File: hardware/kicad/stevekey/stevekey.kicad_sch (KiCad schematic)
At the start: 24 parts, among them J1 ATMEL-ICE-10, J2 Conn_01x04, J3 Conn_01x02, J4 Conn_01x02, J5 Conn_01x02, Q1 2N3904, SW1 SW_SL, SW2 SW_CAPS, SW3 SW_4080, U1 CD4066BM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

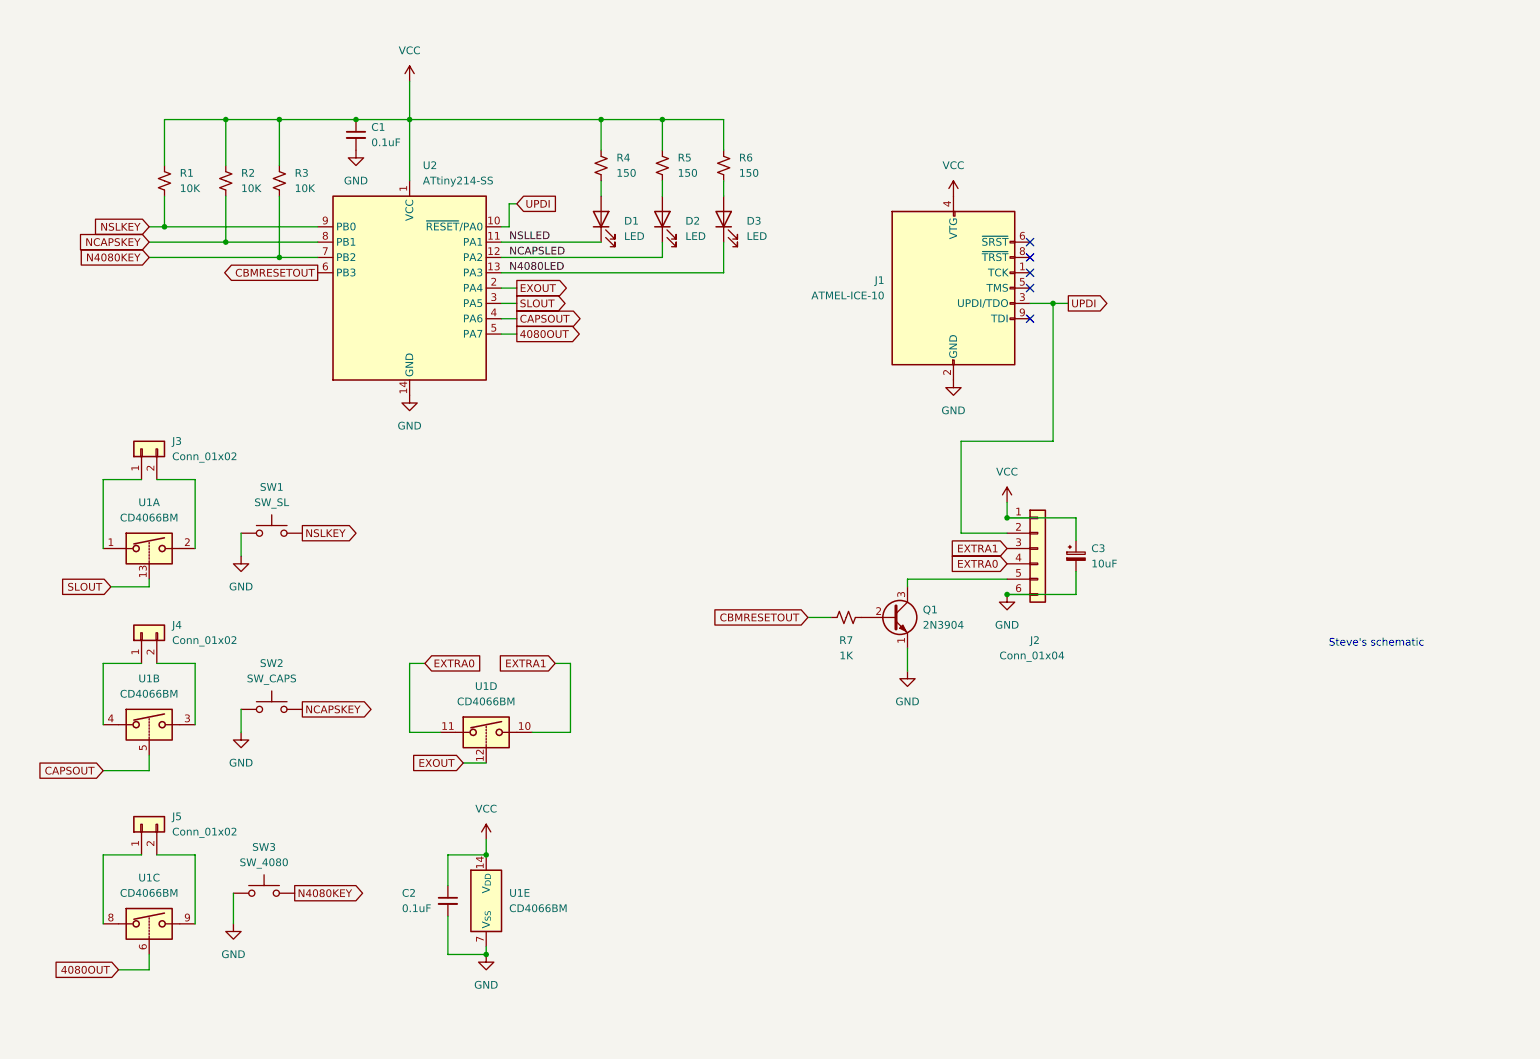
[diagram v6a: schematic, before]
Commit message: Use 330 ohm resistor for LEDs
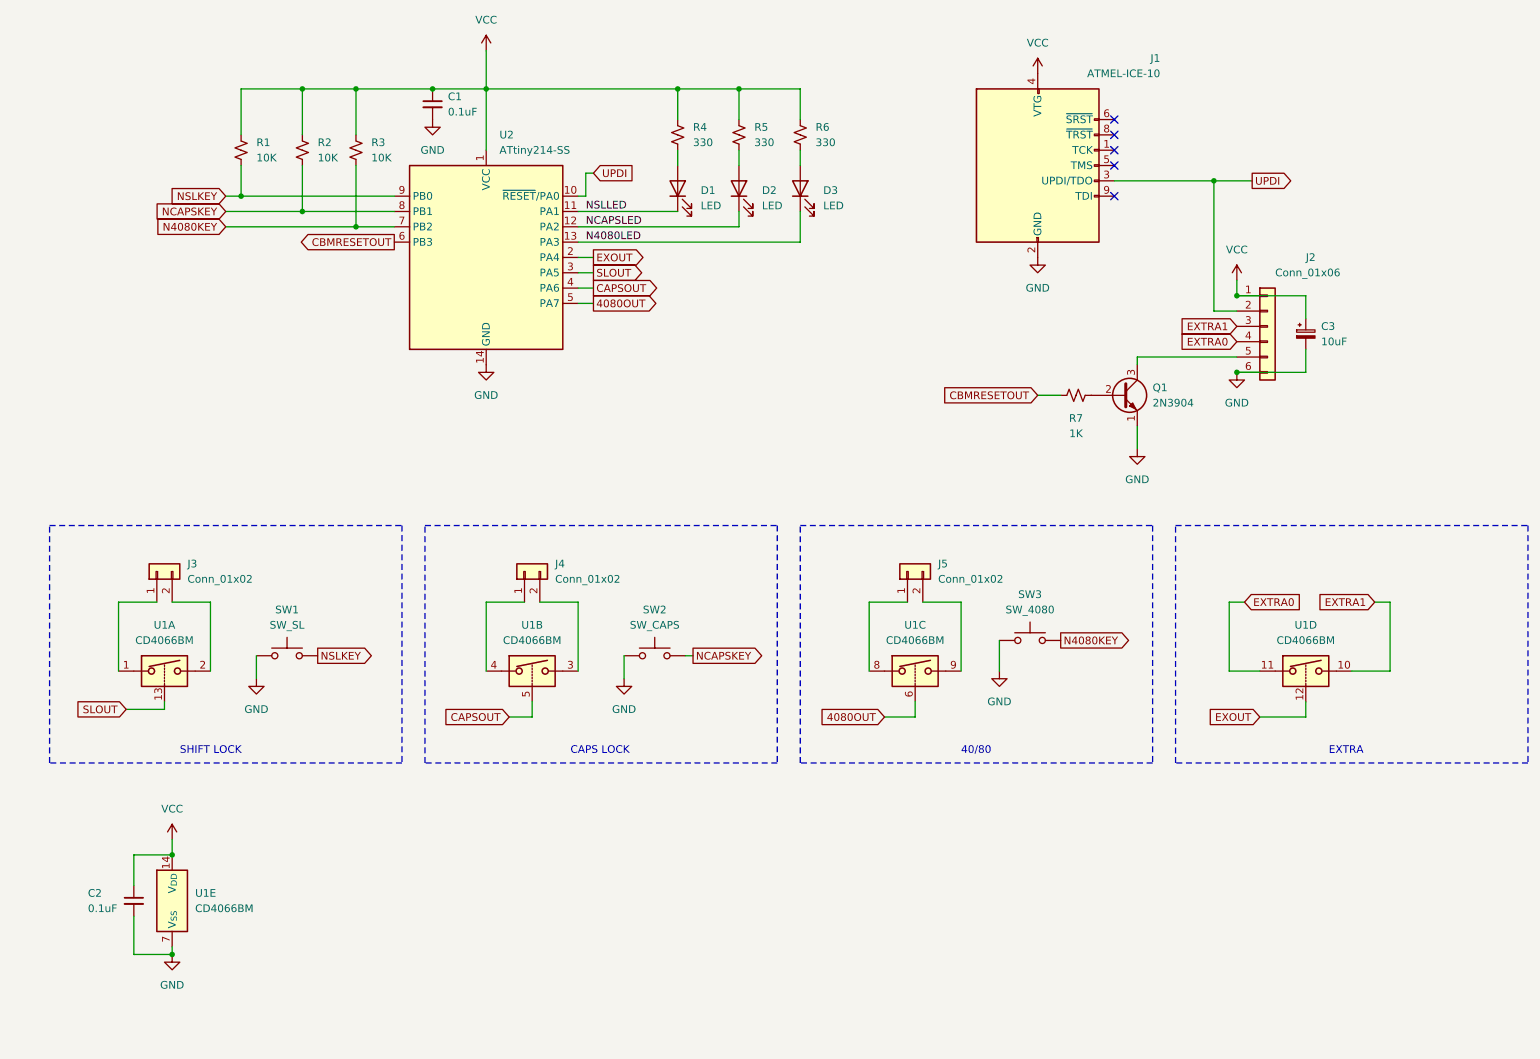
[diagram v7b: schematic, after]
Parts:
- J2: value Conn_01x04 -> Conn_01x06
- R4, R5, R6: value 150 -> 330
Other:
- note added: "40/80"
- note added: "CAPS LOCK"
- note added: "EXTRA"
- note added: "SHIFT LOCK"
- note removed: "Steve's schematic"
- moved on the sheet: C1, C2, C3, D1, D2, D3, J1, J2, J3, J4, J5, Q1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

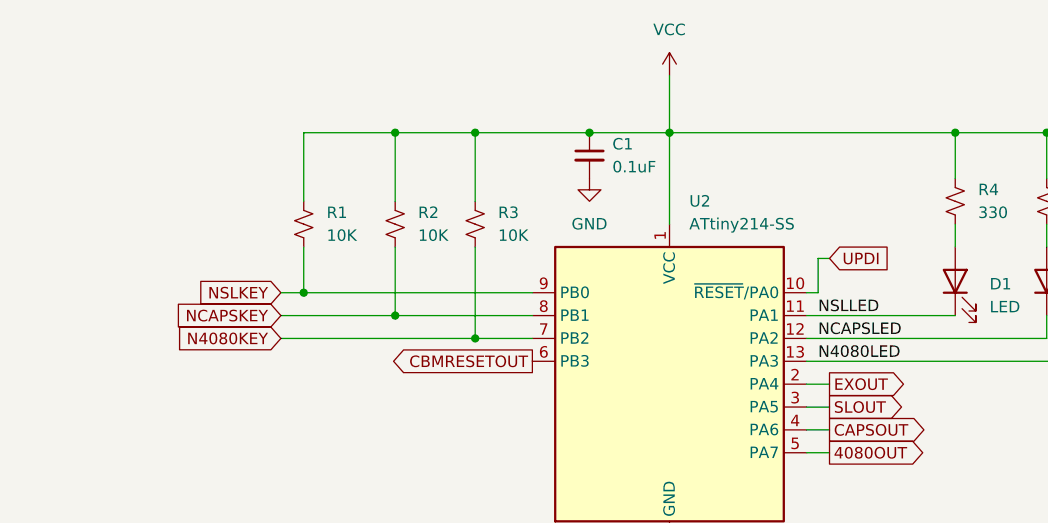
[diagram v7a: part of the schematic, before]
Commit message: Use internal pull-ups for keys
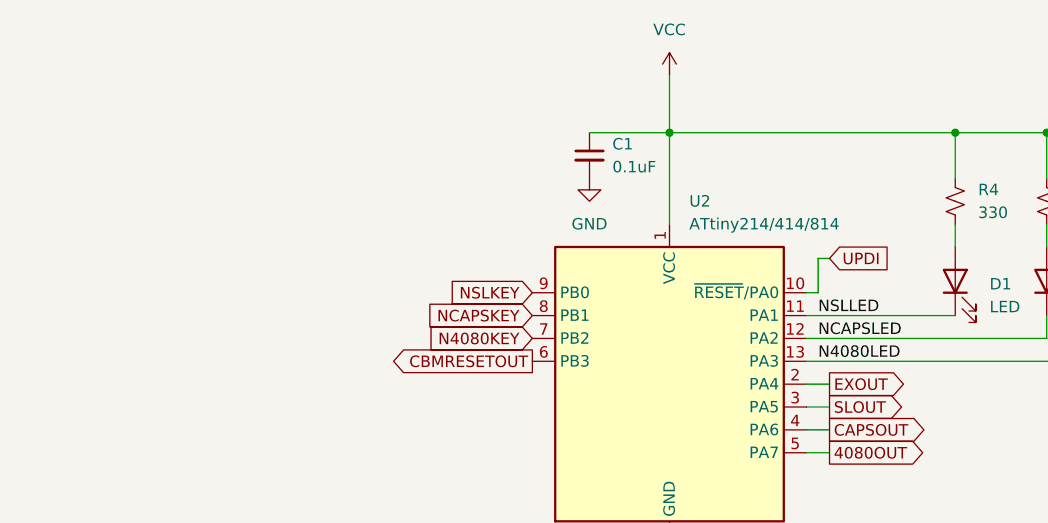
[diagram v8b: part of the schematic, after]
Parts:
- removed R1, R2, R3: 10K, Resistor_THT:R_Axial_DIN0204_L3.6mm_D1.6mm_P7.62mm_Horizontal, symbol Device:R_Small_US
- U2: value ATtiny214-SS -> ATtiny214/414/814
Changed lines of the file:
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@@
 (kicad_sch (version 20230121) (generator eeschema)
   (paper "A4")
-  (junction (at 90.17 31.75) (diameter 0) (color 0 0 0 0)
-  )
   (junction (at 46.99 175.26) (diameter 0) (color 0 0 0 0)
   )
@@
   (junction (at 223.52 66.04) (diameter 0) (color 0 0 0 0)
   )
-  (junction (at 68.58 52.07) (diameter 0) (color 0 0 0 0)
-  )
-  (junction (at 58.42 49.53) (diameter 0) (color 0 0 0 0)
-  )
   (junction (at 219.71 46.99) (diameter 0) (color 0 0 0 0)
   )
-  (junction (at 77.47 54.61) (diameter 0) (color 0 0 0 0)
-  )
   (junction (at 130.81 31.75) (diameter 0) (color 0 0 0 0)
   )
   (junction (at 223.52 78.74) (diameter 0) (color 0 0 0 0)
-  )
-  (junction (at 77.47 31.75) (diameter 0) (color 0 0 0 0)
-  )
-  (junction (at 68.58 31.75) (diameter 0) (color 0 0 0 0)
   )
   (junction (at 46.99 158.75) (diameter 0) (color 0 0 0 0)
@@
     (stroke (width 0) (type default))
   )
-  (wire (pts (xy 55.88 49.53) (xy 58.42 49.53))
-    (stroke (width 0) (type default))
-  )
   (wire (pts (xy 234.95 66.04) (xy 234.95 69.85))
     (stroke (width 0) (type default))
@@
     (stroke (width 0) (type default))
   )
-  (wire (pts (xy 68.58 44.45) (xy 68.58 52.07))
-    (stroke (width 0) (type default))
-  )
   (wire (pts (xy 53.34 128.27) (xy 53.34 116.84))
     (stroke (width 0) (type default))
@@
     (stroke (width 0) (type default))
   )
-  (wire (pts (xy 77.47 31.75) (xy 90.17 31.75))
-    (stroke (width 0) (type default))
-  )
-  (wire (pts (xy 55.88 52.07) (xy 68.58 52.07))
-    (stroke (width 0) (type default))
-  )
   (wire (pts (xy 140.97 31.75) (xy 151.13 31.75))
     (stroke (width 0) (type default))
   )
-  (wire (pts (xy 58.42 44.45) (xy 58.42 49.53))
-    (stroke (width 0) (type default))
-  )
-  (wire (pts (xy 58.42 31.75) (xy 58.42 39.37))
-    (stroke (width 0) (type default))
-  )
   (wire (pts (xy 223.52 66.04) (xy 234.95 66.04))
     (stroke (width 0) (type default))
@@
     (stroke (width 0) (type default))
   )
-  (wire (pts (xy 77.47 31.75) (xy 68.58 31.75))
-    (stroke (width 0) (type default))
-  )
   (wire (pts (xy 222.25 128.27) (xy 227.33 128.27))
     (stroke (width 0) (type default))
@@
     (stroke (width 0) (type default))
   )
-  (wire (pts (xy 58.42 49.53) (xy 83.82 49.53))
-    (stroke (width 0) (type default))
-  )
   (wire (pts (xy 40.64 168.91) (xy 40.64 175.26))
     (stroke (width 0) (type default))
@@
     (stroke (width 0) (type default))
   )
-  (wire (pts (xy 68.58 31.75) (xy 58.42 31.75))
-    (stroke (width 0) (type default))
-  )
-  (wire (pts (xy 55.88 54.61) (xy 77.47 54.61))
-    (stroke (width 0) (type default))
-  )
   (wire (pts (xy 40.64 175.26) (xy 46.99 175.26))
     (stroke (width 0) (type default))
   )
-  (wire (pts (xy 77.47 39.37) (xy 77.47 31.75))
-    (stroke (width 0) (type default))
-  )
   (wire (pts (xy 45.72 133.35) (xy 45.72 134.62))
     (stroke (width 0) (type default))
   )
-  (wire (pts (xy 68.58 31.75) (xy 68.58 39.37))
-    (stroke (width 0) (type default))
-  )
   (wire (pts (xy 121.92 125.73) (xy 121.92 129.54))
     (stroke (width 0) (type default))
@@
     (stroke (width 0) (type default))
   )
-  (wire (pts (xy 68.58 52.07) (xy 83.82 52.07))
-    (stroke (width 0) (type default))
-  )
   (wire (pts (xy 203.2 46.99) (xy 219.71 46.99))
     (stroke (width 0) (type default))
   )
-  (wire (pts (xy 77.47 44.45) (xy 77.47 54.61))
-    (stroke (width 0) (type default))
-  )
   (wire (pts (xy 234.95 78.74) (xy 234.95 74.93))
     (stroke (width 0) (type default))
@@
   )
   (wire (pts (xy 234.95 135.89) (xy 234.95 133.35))
-    (stroke (width 0) (type default))
-  )
-  (wire (pts (xy 77.47 54.61) (xy 83.82 54.61))
     (stroke (width 0) (type default))
   )
@@
     )
   )
-  (global_label "N4080KEY" (shape input) (at 55.88 54.61 180) (fields_autoplaced)
+  (global_label "N4080KEY" (shape input) (at 83.82 54.61 180) (fields_autoplaced)
     (effects (font (size 1.27 1.27)) (justify right))
-    (property "Intersheetrefs" "${INTERSHEET_REFS}" (at 43.2187 54.61 0)
+    (property "Intersheetrefs" "${INTERSHEET_REFS}" (at 71.1587 54.61 0)
       (effects (font (size 1.27 1.27)) (justify right) hide)
     )
@@
     )
   )
-  (global_label "NCAPSKEY" (shape input) (at 55.88 52.07 180) (fields_autoplaced)
+  (global_label "NCAPSKEY" (shape input) (at 83.82 52.07 180) (fields_autoplaced)
     (effects (font (size 1.27 1.27)) (justify right))
-    (property "Intersheetrefs" "${INTERSHEET_REFS}" (at 43.2186 52.07 0)
+    (property "Intersheetrefs" "${INTERSHEET_REFS}" (at 71.1586 52.07 0)
       (effects (font (size 1.27 1.27)) (justify right) hide)
     )
@@
     )
   )
-  (global_label "NSLKEY" (shape input) (at 55.88 49.53 180) (fields_autoplaced)
+  (global_label "NSLKEY" (shape input) (at 83.82 49.53 180) (fields_autoplaced)
     (effects (font (size 1.27 1.27)) (justify right))
-    (property "Intersheetrefs" "${INTERSHEET_REFS}" (at 45.8191 49.53 0)
+    (property "Intersheetrefs" "${INTERSHEET_REFS}" (at 73.7591 49.53 0)
       (effects (font (size 1.27 1.27)) (justify right) hide)
     )
@@
     )
   )
-  (symbol (lib_id "Device:R_Small_US") (at 77.47 41.91 0) (unit 1)
-    (in_bom yes) (on_board yes) (dnp no) (fields_autoplaced)
-    (property "Reference" "R3" (at 80.01 40.64 0)
-      (effects (font (size 1.27 1.27)) (justify left))
-    )
-    (property "Value" "10K" (at 80.01 43.18 0)
-      (effects (font (size 1.27 1.27)) (justify left))
-    )
-    (property "Footprint" "Resistor_THT:R_Axial_DIN0204_L3.6mm_D1.6mm_P7.62mm_Horizontal" (at 77.47 41.91 0)
-      (effects (font (size 1.27 1.27)) hide)
-    )
-    (property "Datasheet" "~" (at 77.47 41.91 0)
-      (effects (font (size 1.27 1.27)) hide)
-    )
-    (pin "1")
-    (pin "2")
-    (instances
-      (project "stevekey"
-        (path "/4393a5c5-44f8-4de9-9c92-ea247f2f7df2"
-          (reference "R3") (unit 1)
-        )
-      )
-    )
-  )
   (symbol (lib_id "Device:R_Small_US") (at 196.85 82.55 90) (unit 1)
     (in_bom yes) (on_board yes) (dnp no)
@@
       (effects (font (size 1.27 1.27)) (justify left))
     )
-    (property "Value" "ATtiny214-SS" (at 101.2541 41.91 0)
+    (property "Value" "ATtiny214/414/814" (at 101.2541 41.91 0)
       (effects (font (size 1.27 1.27)) (justify left))
     )
@@
     )
   )
-  (symbol (lib_id "Device:R_Small_US") (at 68.58 41.91 0) (unit 1)
-    (in_bom yes) (on_board yes) (dnp no) (fields_autoplaced)
-    (property "Reference" "R2" (at 71.12 40.64 0)
-      (effects (font (size 1.27 1.27)) (justify left))
-    )
-    (property "Value" "10K" (at 71.12 43.18 0)
-      (effects (font (size 1.27 1.27)) (justify left))
-    )
-    (property "Footprint" "Resistor_THT:R_Axial_DIN0204_L3.6mm_D1.6mm_P7.62mm_Horizontal" (at 68.58 41.91 0)
-      (effects (font (size 1.27 1.27)) hide)
-    )
-    (property "Datasheet" "~" (at 68.58 41.91 0)
-      (effects (font (size 1.27 1.27)) hide)
-    )
-    (pin "1")
-    (pin "2")
-    (instances
-      (project "stevekey"
-        (path "/4393a5c5-44f8-4de9-9c92-ea247f2f7df2"
-          (reference "R2") (unit 1)
-        )
-      )
-    )
-  )
   (symbol (lib_id "Device:LED") (at 151.13 48.26 90) (unit 1)
     (in_bom yes) (on_board yes) (dnp no) (fields_autoplaced)
@@
         )
       )
-    )
-  )
-  (symbol (lib_id "Device:R_Small_US") (at 58.42 41.91 0) (unit 1)
-    (in_bom yes) (on_board yes) (dnp no) (fields_autoplaced)
-    (property "Reference" "R1" (at 60.96 40.64 0)
-      (effects (font (size 1.27 1.27)) (justify left))
-    )
-    (property "Value" "10K" (at 60.96 43.18 0)
-      (effects (font (size 1.27 1.27)) (justify left))
-    )
-    (property "Footprint" "Resistor_THT:R_Axial_DIN0204_L3.6mm_D1.6mm_P7.62mm_Horizontal" (at 58.42 41.91 0)
-      (effects (font (size 1.27 1.27)) hide)
-    )
-    (property "Datasheet" "~" (at 58.42 41.91 0)
-      (effects (font (size 1.27 1.27)) hide)
-    )
-    (pin "1")
-    (pin "2")
-    (instances
-      (project "stevekey"
-        (path "/4393a5c5-44f8-4de9-9c92-ea247f2f7df2"
-          (reference "R1") (unit 1)
-        )
-      )
